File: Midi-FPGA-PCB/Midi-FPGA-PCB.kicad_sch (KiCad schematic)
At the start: 5 parts, among them U1 ESP32-WROOM-32

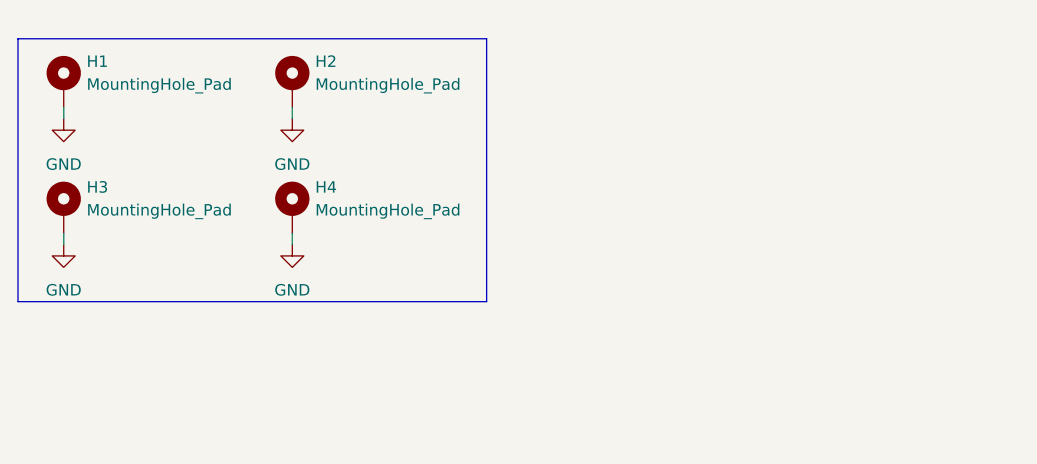
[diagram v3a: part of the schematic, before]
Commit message: Created LDO circuit
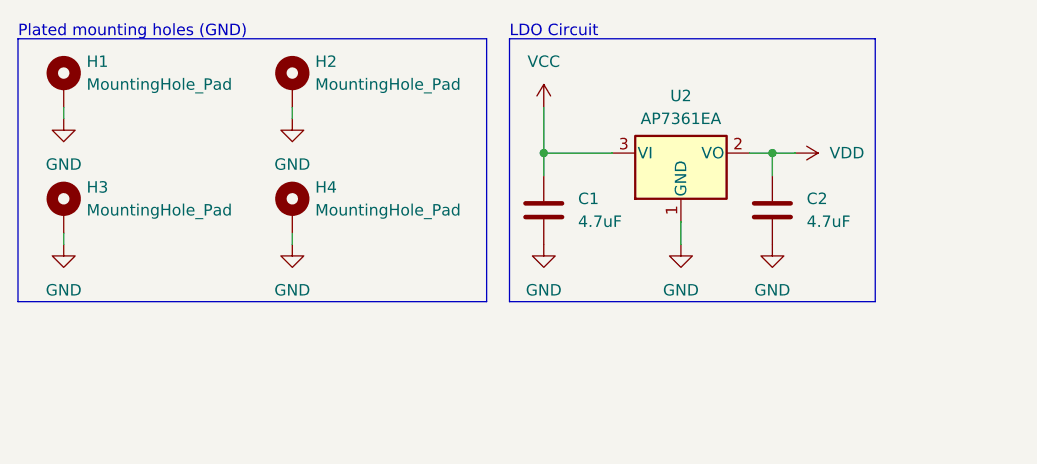
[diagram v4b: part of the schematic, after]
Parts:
- added C1, C2: 4.7uF, symbol Device:C
- added U2: AP7361EA, Midi-FPGA-lib:SOT-223-3R, symbol Regulator_Linear:AP7361C-33E
- U1: Store page https://www.digikey.co.uk/en/products/detail/espressif-syst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 -> (none); URL (none) -> https://www.digikey.co.uk/en/products/detail/espressif-syst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
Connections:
- net GND: now also C1.2, C2.2, U2.1 (GND)
- new net VCC: C1.1, U2.3 (VI)
- new net VDD: C2.1, U2.2 (VO)
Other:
- note added: "LDO Circuit"
- note added: "Plated mounting holes (GND)"
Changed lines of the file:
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@@
     (rev "1.0")
   )
+  (junction (at 73.66 27.94) (diameter 0) (color 0 0 0 0)
+  )
+  (junction (at 99.06 27.94) (diameter 0) (color 0 0 0 0)
+  )
+  (wire (pts (xy 99.06 27.94) (xy 99.06 30.48))
+    (stroke (width 0) (type default))
+  )
   (wire (pts (xy 20.32 22.86) (xy 20.32 24.13))
     (stroke (width 0) (type default))
   )
+  (wire (pts (xy 73.66 22.86) (xy 73.66 27.94))
+    (stroke (width 0) (type default))
+  )
   (wire (pts (xy 45.72 38.1) (xy 45.72 36.83))
     (stroke (width 0) (type default))
@@
     (stroke (width 0) (type default))
   )
+  (wire (pts (xy 88.9 35.56) (xy 88.9 38.1))
+    (stroke (width 0) (type default))
+  )
+  (wire (pts (xy 99.06 27.94) (xy 101.6 27.94))
+    (stroke (width 0) (type default))
+  )
+  (wire (pts (xy 96.52 27.94) (xy 99.06 27.94))
+    (stroke (width 0) (type default))
+  )
+  (wire (pts (xy 73.66 27.94) (xy 73.66 30.48))
+    (stroke (width 0) (type default))
+  )
   (wire (pts (xy 20.32 38.1) (xy 20.32 36.83))
     (stroke (width 0) (type default))
   )
+  (wire (pts (xy 73.66 27.94) (xy 81.28 27.94))
+    (stroke (width 0) (type default))
+  )
   (wire (pts (xy 45.72 22.86) (xy 45.72 24.13))
     (stroke (width 0) (type default))
@@
     (fill (type none))
   )
+  (rectangle (start 69.85 15.24) (end 110.49 44.45)
+    (stroke (width 0) (type default))
+    (fill (type none))
+  )
+  (text "Plated mounting holes (GND)" (at 15.24 15.24 0)
+    (effects (font (size 1.27 1.27)) (justify left bottom))
+  )
+  (text "LDO Circuit" (at 69.85 15.24 0)
+    (effects (font (size 1.27 1.27)) (justify left bottom))
+  )
+  (symbol (lib_id "Regulator_Linear:AP7361C-33E") (at 88.9 27.94 0) (unit 1)
+    (in_bom yes) (on_board yes) (dnp no) (fields_autoplaced)
+    (property "Reference" "U2" (at 88.9 21.59 0)
+      (effects (font (size 1.27 1.27)))
+    )
+    (property "Value" "AP7361EA" (at 88.9 24.13 0)
+      (effects (font (size 1.27 1.27)))
+    )
+    (property "Footprint" "Midi-FPGA-lib:SOT-223-3R" (at 88.9 22.225 0)
+      (effects (font (size 1.27 1.27) italic) hide)
+    )
+    (property "Datasheet" "https://www.diodes.com/assets/Datasheets/AP7361EA.pdf" (at 88.9 29.21 0)
+      (effects (font (size 1.27 1.27)) hide)
+    )
+    (property "URL" "https://www.digikey.co.uk/en/products/detail/diodes-incorporated/AP7361EA-33ER-13/16547698" (at 88.9 27.94 0)
+      (effects (font (size 1.27 1.27)) hide)
+    )
+    (pin "3")
+    (pin "1")
+    (pin "2")
+    (instances
+      (project "Midi-FPGA-PCB"
+        (path "/75ad38e9-b0d3-45bc-bcac-026c9800f4ea"
+          (reference "U2") (unit 1)
+        )
+      )
+    )
+  )
   (symbol (lib_id "Mechanical:MountingHole_Pad") (at 45.72 34.29 0) (unit 1)
     (in_bom yes) (on_board yes) (dnp no) (fields_autoplaced)
@@
     )
   )
+  (symbol (lib_id "Device:C") (at 99.06 34.29 0) (unit 1)
+    (in_bom yes) (on_board yes) (dnp no) (fields_autoplaced)
+    (property "Reference" "C2" (at 102.87 33.02 0)
+      (effects (font (size 1.27 1.27)) (justify left))
+    )
+    (property "Value" "4.7uF" (at 102.87 35.56 0)
+      (effects (font (size 1.27 1.27)) (justify left))
+    )
+    (property "Footprint" "" (at 100.0252 38.1 0)
+      (effects (font (size 1.27 1.27)) hide)
+    )
+    (property "Datasheet" "https://search.murata.co.jp/Ceramy/image/img/A01X/G101/ENG/GRM21BR71C475KE51-01.pdf" (at 99.06 34.29 0)
+      (effects (font (size 1.27 1.27)) hide)
+    )
+    (property "URL" "https://www.digikey.co.uk/en/products/detail/murata-electronics/GRM21BR71C475KE51L/6606095" (at 99.06 34.29 0)
+      (effects (font (size 1.27 1.27)) hide)
+    )
+    (pin "1")
+    (pin "2")
+    (instances
+      (project "Midi-FPGA-PCB"
+        (path "/75ad38e9-b0d3-45bc-bcac-026c9800f4ea"
+          (reference "C2") (unit 1)
+        )
+      )
+    )
+  )
   (symbol (lib_id "Mechanical:MountingHole_Pad") (at 45.72 20.32 0) (unit 1)
     (in_bom yes) (on_board yes) (dnp no) (fields_autoplaced)
@@
     )
   )
+  (symbol (lib_id "power:GND") (at 88.9 38.1 0) (unit 1)
+    (in_bom yes) (on_board yes) (dnp no) (fields_autoplaced)
+    (property "Reference" "#PWR08" (at 88.9 44.45 0)
+      (effects (font (size 1.27 1.27)) hide)
+    )
+    (property "Value" "GND" (at 88.9 43.18 0)
+      (effects (font (size 1.27 1.27)))
+    )
+    (property "Footprint" "" (at 88.9 38.1 0)
+      (effects (font (size 1.27 1.27)) hide)
+    )
+    (property "Datasheet" "" (at 88.9 38.1 0)
+      (effects (font (size 1.27 1.27)) hide)
+    )
+    (pin "1")
+    (instances
+      (project "Midi-FPGA-PCB"
+        (path "/75ad38e9-b0d3-45bc-bcac-026c9800f4ea"
+          (reference "#PWR08") (unit 1)
+        )
+      )
+    )
+  )
+  (symbol (lib_id "power:VDD") (at 101.6 27.94 270) (unit 1)
+    (in_bom yes) (on_board yes) (dnp no) (fields_autoplaced)
+    (property "Reference" "#PWR07" (at 97.79 27.94 0)
+      (effects (font (size 1.27 1.27)) hide)
+    )
+    (property "Value" "VDD" (at 105.41 27.94 90)
+      (effects (font (size 1.27 1.27)) (justify left))
+    )
+    (property "Footprint" "" (at 101.6 27.94 0)
+      (effects (font (size 1.27 1.27)) hide)
+    )
+    (property "Datasheet" "" (at 101.6 27.94 0)
+      (effects (font (size 1.27 1.27)) hide)
+    )
+    (pin "1")
+    (instances
+      (project "Midi-FPGA-PCB"
+        (path "/75ad38e9-b0d3-45bc-bcac-026c9800f4ea"
+          (reference "#PWR07") (unit 1)
+        )
+      )
+    )
+  )
   (symbol (lib_id "power:GND") (at 45.72 24.13 0) (unit 1)
     (in_bom yes) (on_board yes) (dnp no) (fields_autoplaced)
@@
     )
   )
+  (symbol (lib_id "power:VCC") (at 73.66 22.86 0) (unit 1)
+    (in_bom yes) (on_board yes) (dnp no) (fields_autoplaced)
+    (property "Reference" "#PWR06" (at 73.66 26.67 0)
+      (effects (font (size 1.27 1.27)) hide)
+    )
+    (property "Value" "VCC" (at 73.66 17.78 0)
+      (effects (font (size 1.27 1.27)))
+    )
+    (property "Footprint" "" (at 73.66 22.86 0)
+      (effects (font (size 1.27 1.27)) hide)
+    )
+    (property "Datasheet" "" (at 73.66 22.86 0)
+      (effects (font (size 1.27 1.27)) hide)
+    )
+    (pin "1")
+    (instances
+      (project "Midi-FPGA-PCB"
+        (path "/75ad38e9-b0d3-45bc-bcac-026c9800f4ea"
+          (reference "#PWR06") (unit 1)
+        )
+      )
+    )
+  )
   (symbol (lib_id "Midi-FGPA-lib:ESP32-WROOM-32_(No_Thermal)") (at 139.7 97.79 0) (unit 1)
     (in_bom yes) (on_board yes) (dnp no) (fields_autoplaced)
@@
       (effects (font (size 1.27 1.27)) hide)
     )
-    (property "Store page" "https://www.digikey.co.uk/en/products/detail/espressif-systems/ESP32-WROOM-32E-N4/11613125" (at 139.7 97.79 0)
+    (property "URL" "https://www.digikey.co.uk/en/products/detail/espressif-systems/ESP32-WROOM-32E-N4/11613125" (at 139.7 97.79 0)
       (effects (font (size 1.27 1.27)) hide)
     )
@@
     )
   )
+  (symbol (lib_id "power:GND") (at 73.66 38.1 0) (unit 1)
+    (in_bom yes) (on_board yes) (dnp no) (fields_autoplaced)
+    (property "Reference" "#PWR09" (at 73.66 44.45 0)
+      (effects (font (size 1.27 1.27)) hide)
+    )
+    (property "Value" "GND" (at 73.66 43.18 0)
+      (effects (font (size 1.27 1.27)))
+    )
+    (property "Footprint" "" (at 73.66 38.1 0)
+      (effects (font (size 1.27 1.27)) hide)
+    )
+    (property "Datasheet" "" (at 73.66 38.1 0)
+      (effects (font (size 1.27 1.27)) hide)
+    )
+    (pin "1")
+    (instances
+      (project "Midi-FPGA-PCB"
+        (path "/75ad38e9-b0d3-45bc-bcac-026c9800f4ea"
+          (reference "#PWR09") (unit 1)
+        )
+      )
+    )
+  )
   (symbol (lib_id "Mechanical:MountingHole_Pad") (at 20.32 20.32 0) (unit 1)
     (in_bom yes) (on_board yes) (dnp no) (fields_autoplaced)
@@
     )
   )
+  (symbol (lib_id "Device:C") (at 73.66 34.29 0) (unit 1)
+    (in_bom yes) (on_board yes) (dnp no) (fields_autoplaced)
+    (property "Reference" "C1" (at 77.47 33.02 0)
+      (effects (font (size 1.27 1.27)) (justify left))
+    )
+    (property "Value" "4.7uF" (at 77.47 35.56 0)
+      (effects (font (size 1.27 1.27)) (justify left))
+    )
+    (property "Footprint" "" (at 74.6252 38.1 0)
+      (effects (font (size 1.27 1.27)) hide)
+    )
+    (property "Datasheet" "https://search.murata.co.jp/Ceramy/image/img/A01X/G101/ENG/GRM21BR71C475KE51-01.pdf" (at 73.66 34.29 0)
+      (effects (font (size 1.27 1.27)) hide)
+    )
+    (property "URL" "https://www.digikey.co.uk/en/products/detail/murata-electronics/GRM21BR71C475KE51L/6606095" (at 73.66 34.29 0)
+      (effects (font (size 1.27 1.27)) hide)
+    )
+    (pin "1")
+    (pin "2")
+    (instances
+      (project "Midi-FPGA-PCB"
+        (path "/75ad38e9-b0d3-45bc-bcac-026c9800f4ea"
+          (reference "C1") (unit 1)
+        )
+      )
+    )
+  )
   (symbol (lib_id "Mechanical:MountingHole_Pad") (at 20.32 34.29 0) (unit 1)
     (in_bom yes) (on_board yes) (dnp no) (fields_autoplaced)
@@
         )
       )
+    )
+  )
+  (symbol (lib_id "power:GND") (at 99.06 38.1 0) (unit 1)
+    (in_bom yes) (on_board yes) (dnp no) (fields_autoplaced)
+    (property "Reference" "#PWR010" (at 99.06 44.45 0)
+      (effects (font (size 1.27 1.27)) hide)
+    )
+    (property "Value" "GND" (at 99.06 43.18 0)
+      (effects (font (size 1.27 1.27)))
+    )
+    (property "Footprint" "" (at 99.06 38.1 0)
+      (effects (font (size 1.27 1.27)) hide)
+    )
+    (property "Datasheet" "" (at 99.06 38.1 0)
+      (effects (font (size 1.27 1.27)) hide)
+    )
+    (pin "1")
+    (instances
+      (project "Midi-FPGA-PCB"
+        (path "/75ad38e9-b0d3-45bc-bcac-026c9800f4ea"
+          (reference "#PWR010") (unit 1)
+        )
+      )

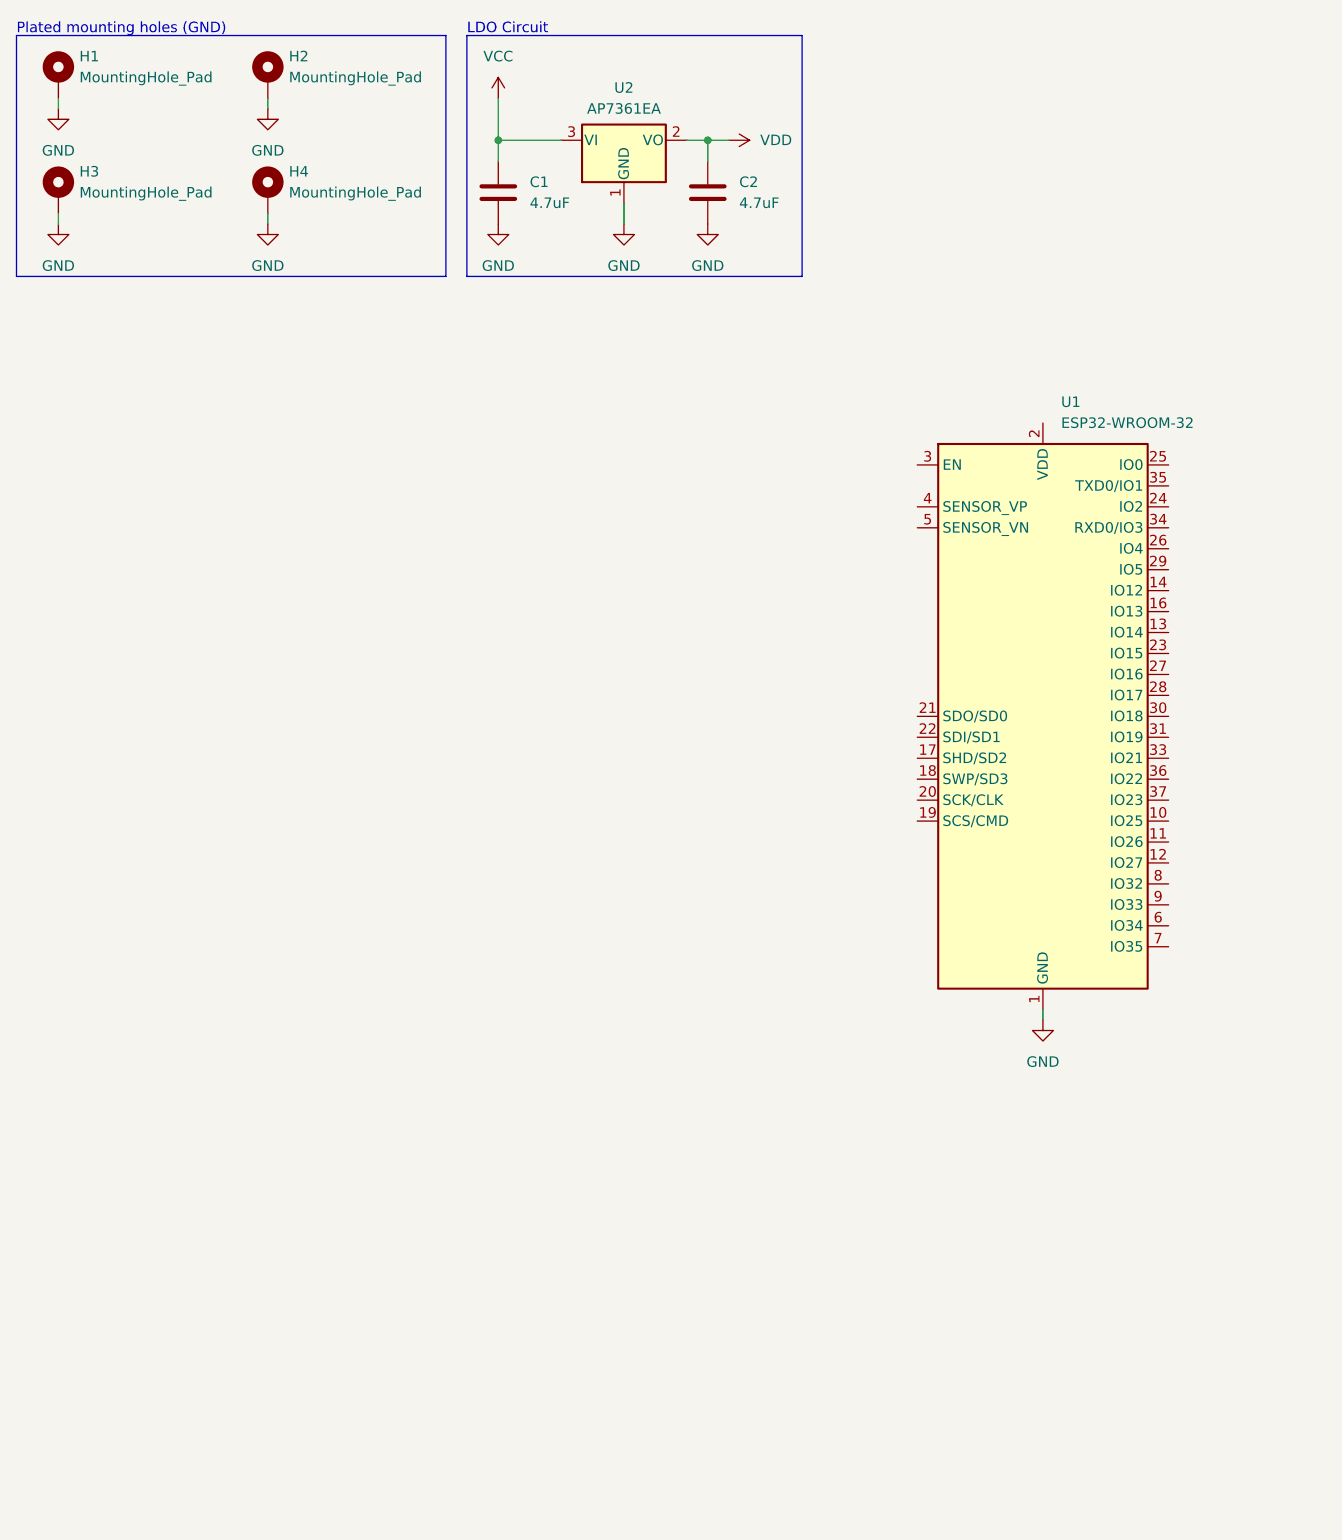
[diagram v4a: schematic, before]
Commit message: Created LDO circuitry
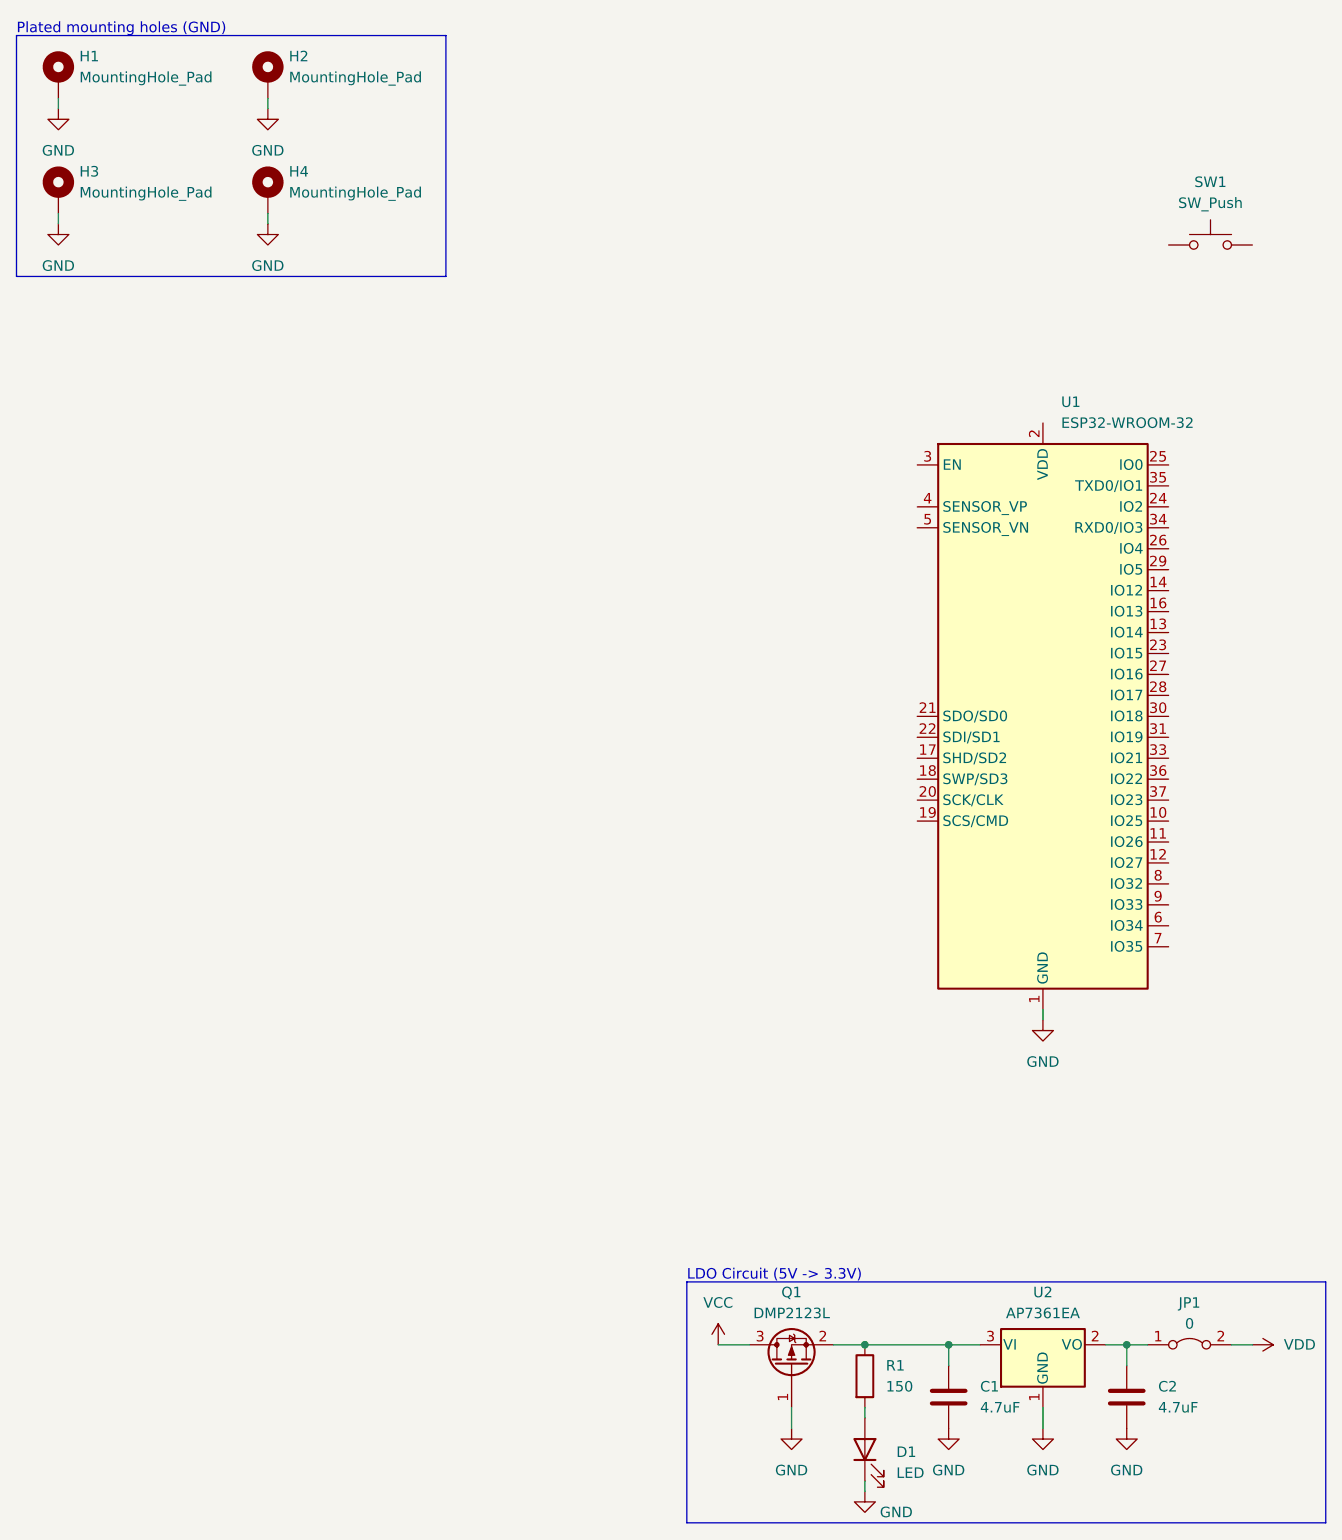
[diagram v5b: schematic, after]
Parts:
- added D1: LED, LED_SMD:LED_0603_1608Metric_Pad1.05x0.95mm_HandSolder, symbol Device:LED
- added JP1: 0, Resistor_SMD:R_0805_2012Metric_Pad1.20x1.40mm_HandSolder, symbol Jumper:Jumper_2_Bridged
- added Q1: DMP2123L, Package_TO_SOT_SMD:SOT-23-3, symbol Device:Q_PMOS_GSD
- added R1: 150, Resistor_SMD:R_0805_2012Metric_Pad1.20x1.40mm_HandSolder, symbol Device:R
- added SW1: SW_Push, symbol Switch:SW_Push
- C1, C2: footprint (none) -> Capacitor_SMD:C_0805_2012Metric_Pad1.18x1.45mm_HandSolder
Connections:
- net GND: now also D1.1 (K), Q1.1 (G)
- net VCC: now also Q1.3 (D); no longer C1.1, U2.3 (VI)
- net VDD: now also JP1.2 (B); no longer C2.1, U2.2 (VO)
- new net: C2.1, JP1.1 (A), U2.2 (VO)
- new net: C1.1, Q1.2 (S), R1.1, U2.3 (VI)
- new net: D1.2 (A), R1.2
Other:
- note added: "LDO Circuit (5V -> 3.3V)"
- note removed: "LDO Circuit"
- moved on the sheet: C1, U2
